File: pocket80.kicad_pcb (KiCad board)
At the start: 4 copper layers, 68.6 x 107.3 mm, 136 parts, among them J1 USB_C_Receptacle_USB2.0_14P, J2 Conn_02x10_Odd_Even, Q1 IRLML6402, Q2 BC847, SW1 F1, SW10 4, SW11 9, SW12 5, SW13 A, SW14 6, SW15 B, SW16 7, SW17 0, SW18 INC, SW19 1, SW2 F2, SW20 DEC, SW21 2, SW22 SEL, SW23 3, SW24 GO!, SW25 SW_Push_DPDT, SW26 RESET, SW3 F3, SW4 F4, SW5 C, SW6 D, SW7 E, SW8 F, SW9 8, U1 Z80CPU, U10 74HC00, U11 74HC138, U12 CH340N, U13 TP4056-42-ESOP8, U14 SX1308, U15 LM393, U16 74HC74, U17 28C256, U2 74HC244, U3 PIO-PLCC-44, U4 SIO3-PLCC-44, U5 CTC-PLCC-44, U6 NE555D, U7 74HC04, U8 62256, U9 24C512, Y1 3.6864M

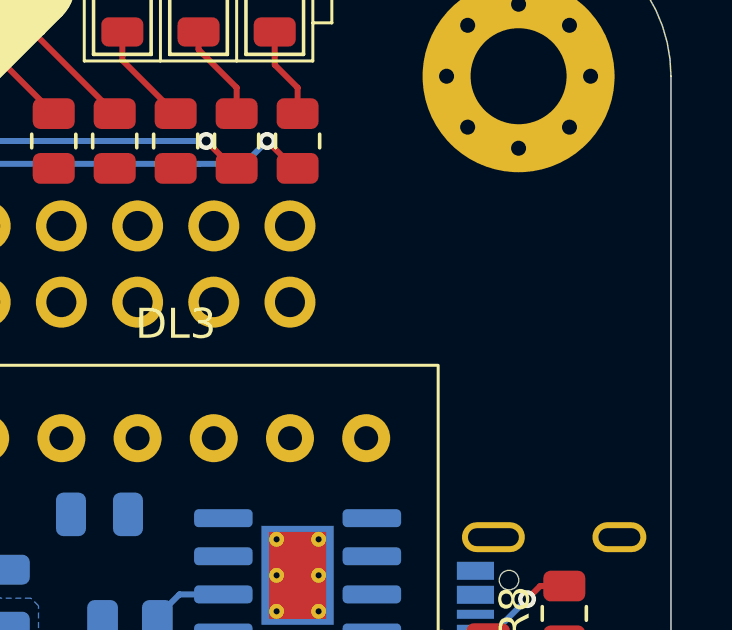
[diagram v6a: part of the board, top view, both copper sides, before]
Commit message: HW: Add LiPo connector
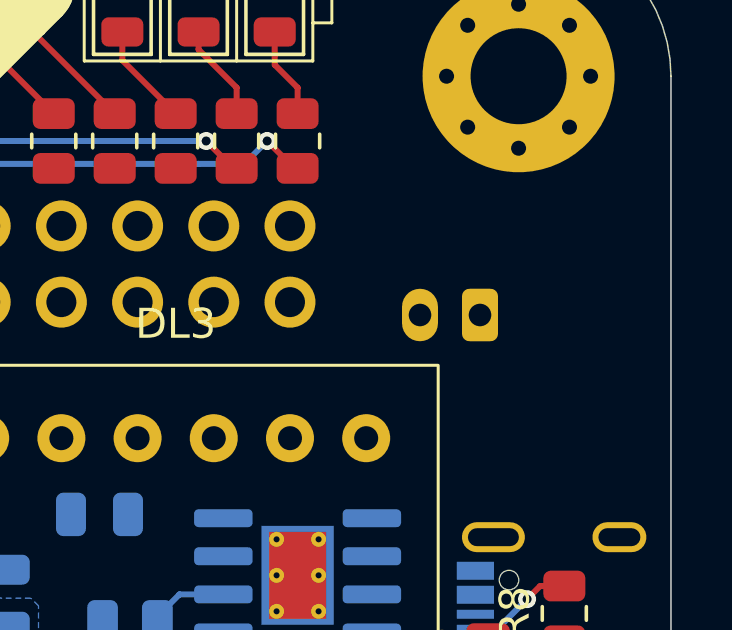
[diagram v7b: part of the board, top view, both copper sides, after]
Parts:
- added J3: Conn_01x02, Connector_JST:JST_PH_B2B-PH-K_1x02_P2.00mm_Vertical, B.Cu at (158.7, 48.2)

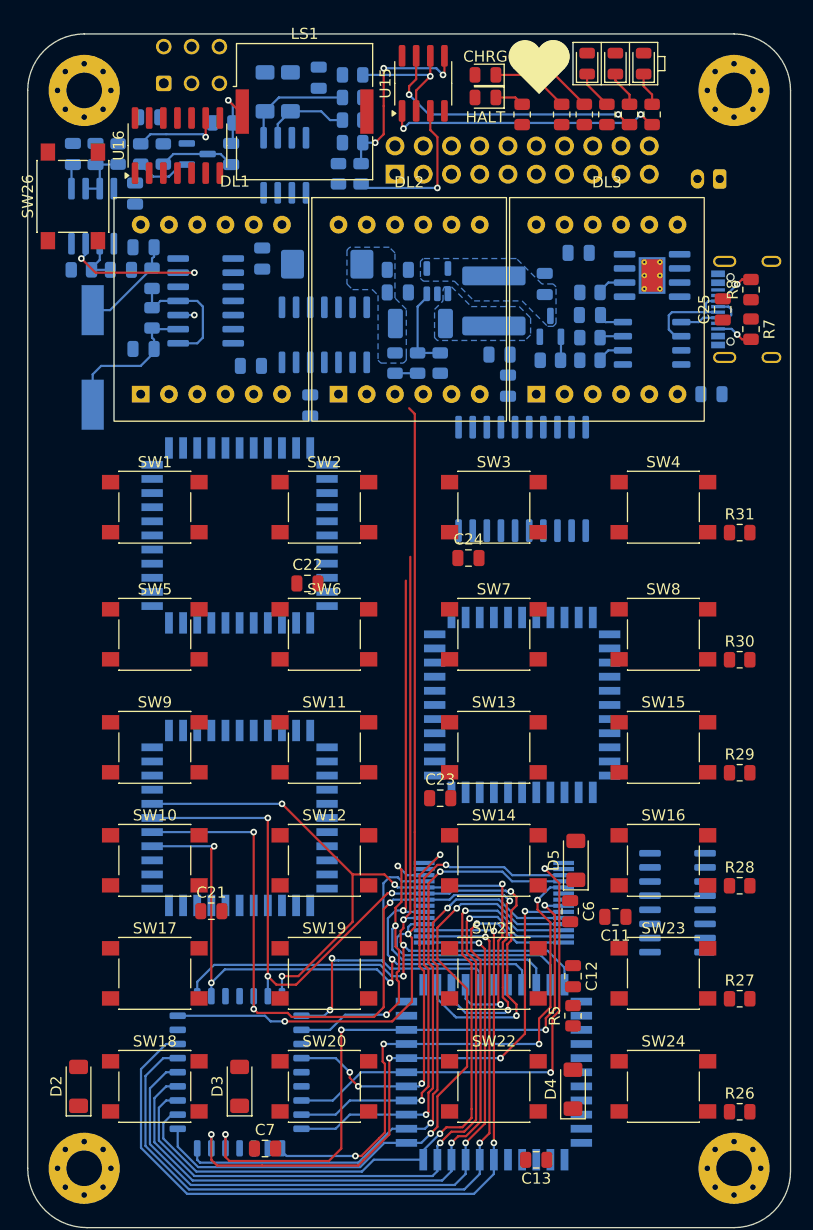
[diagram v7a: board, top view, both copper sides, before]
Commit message: HW: Initial power routing
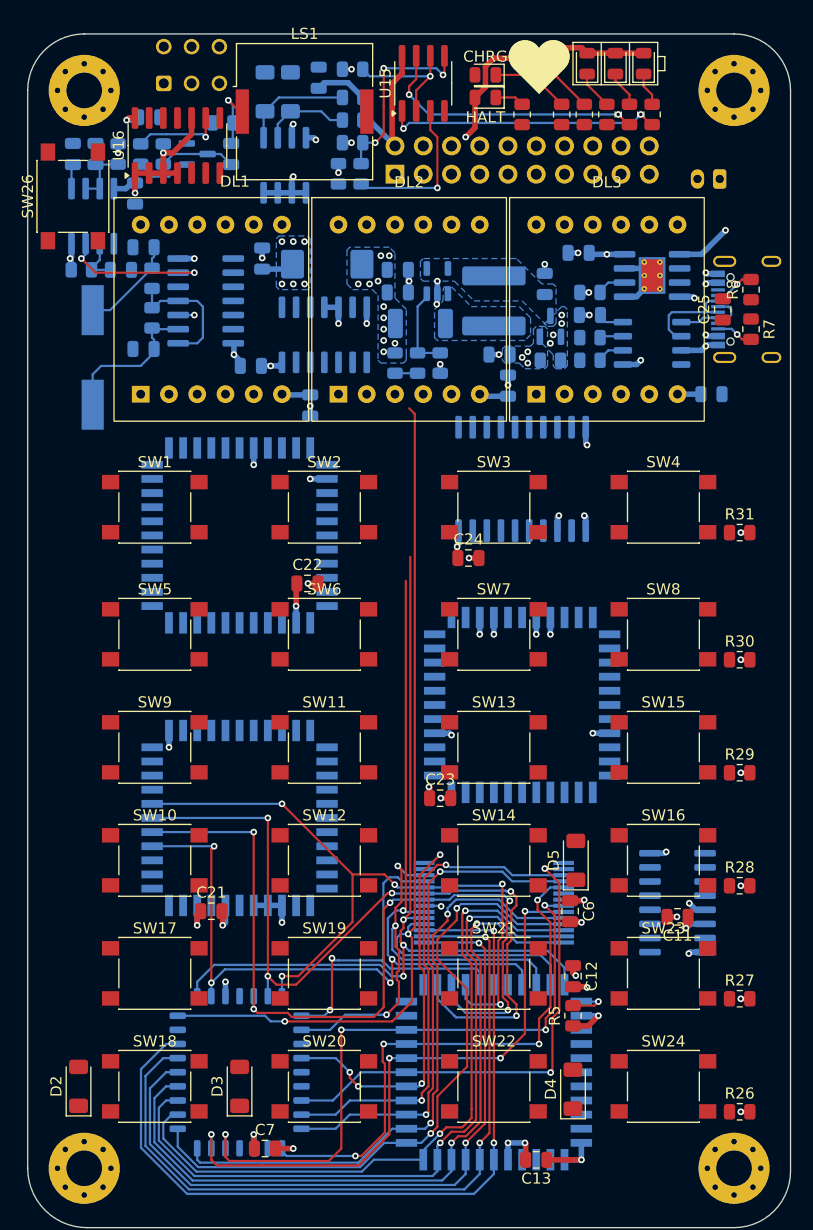
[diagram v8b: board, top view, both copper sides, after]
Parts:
- moved C11 5.59 mm to (154.9, 114.6)
- moved R21 0.51 mm to (125.7, 38.4)
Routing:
- net VCC: track 0.00 -> 116.4 mm, vias 0 -> 41
- net GND: track 0.00 -> 77.8 mm, vias 0 -> 50
- net VBUS: track 0.00 -> 8.68 mm, vias 0 -> 5
- net +BATT: track 0.00 -> 5.84 mm, vias 0 -> 5
- net /CPU/~{INT}: track 0.00 -> 3.97 mm, vias 0 -> 1
- net Net-(Q1-G): track 2.13 -> 0.00 mm, vias 0 -> 4
- added copper zone on B.Cu, net +BATT
- added copper zone on In1.Cu, net +BATT
- added copper zone on B.Cu, net GND
- added copper zone on In2.Cu, net GND
- added copper zone on B.Cu, net Net-(Q1-G)
- added copper zone on In1.Cu, net Net-(Q1-G)
- added copper zone on In1.Cu, net VBUS
- added copper zone on In1.Cu, net VCC
